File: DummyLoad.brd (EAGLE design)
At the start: 101.6 x 76.2 mm, 16 parts, among them IC1 LM358, J1 BINDING-POST, J2 BINDING-POST, Q1 NTE2390-OFFBOARD, SW1 SWITCH-SPDT, X1 SCREW-TERM-2

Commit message: Rough layout
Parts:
- removed X1: SCREW-TERM-2, SaintGimp:SCREW-TERM-2
- added C4: 100uF, SaintGimp:CAP-POL-5-8
- added C5: 2.2uF, SaintGimp:CAP-POL-2.5-5
- added D1: LED, SaintGimp:LED5MM
- added J10, J3, J4, J5, J7, J8, J9: PINHD-1X1, SaintGimp:1X01
- added J6: POWERJACK-OFFBRD, SaintGimp:1X03
- added R10: 47K, SaintGimp:AXIAL-7.5MM
- added R7: 1M, SaintGimp:AXIAL-7.5MM
- added R8: 4K7, SaintGimp:AXIAL-7.5MM
- added R9: (no value), SaintGimp:AXIAL-7.5MM
- added RV2, RV3: 5K, SaintGimp:TRIM_POT
- added SW2: SWITCH-SPDT-OFFBRD, SaintGimp:1X03
- added U$1: PANEL-METER-OFFBRD, SaintGimp:1X04
- added U1: LP2950, SaintGimp:TO92-INLINE
- Q1: value NTE2390-OFFBOARD -> NTE2390; device SaintGimp:SCREW-TERM-3 -> SaintGimp:TO220BV
- R3: value 12K -> 180K
- R4: value 3.3K -> 4K7
- R5: value 1R -> 0R1; device SaintGimp:SCREW-TERM-2 -> SaintGimp:AXIAL-7.5MM
- R6: value 150R -> 68K
- RV1: device SaintGimp:POT-PCB-MOUNT -> SaintGimp:1X03
- SW1: value SWITCH-SPDT -> SWITCH-SPDT-OFFBRD; device SaintGimp:SWITCH-SPDT -> SaintGimp:1X03
- moved R4 65.9 mm to (11.4, 10.2)
- moved R3 54.6 mm to (30.5, 11.4), turned to 90 degrees
- moved J1 50.2 mm to (59.7, 11.4)
- moved J2 50.2 mm to (58.4, 33.0)
- moved R2 41.6 mm to (33.0, 11.4), turned to 90 degrees
- moved R1 39.5 mm to (11.4, 12.7), turned to 180 degrees
- moved SW1 37.4 mm to (17.8, 3.81)
- moved R6 37.1 mm to (11.4, 20.3)
- moved C1 35.9 mm to (21.6, 7.62)
- moved Q1 31.0 mm to (76.2, 26.7), turned to 270 degrees
- moved IC1 27.3 mm to (22.9, 14.0)
- moved R5 26.9 mm to (74.9, 15.2)
- moved C3 19.0 mm to (35.6, 11.4), turned to 270 degrees
- moved C2 18.1 mm to (21.6, 20.3)
- moved RV1 8.03 mm to (38.1, 3.81), turned to 0 degrees
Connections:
- removed net N$2 (its old number): Q1.1, R1.P$2
- new net +5V: C2.1, C5.+, D1.A, IC1.8, J7.1, RV1.3, U$1.1, U1.1
- new net GATE: J3.1, Q1.P1, R1.P$2, R7.P$1
- new net METER: IC1.7, J10.1, R6.P$2, U$1.3
- new net N$12: R8.P$1, RV3.2
- new net N$13: IC1.3, R3.P$2, SW1.2
- new net N$4: D1.K, R9.P$1
- new net SENSE: IC1.5, J4.1, Q1.P3, R2.P$2, R5.P$2
- net GND: now also C4.-, C5.-, J5.1, J6.2, J6.3, J8.1, J9.1, R10.P$1, R5.P$1, R7.P$2, R9.P$2, RV1.1, RV2.1, RV2.3, RV3.1, RV3.3, U$1.2, U$1.4, U1.2; no longer IC1.5, R5.1, R6.P$1, RV1.P$1, X1.2
- net N$1: now also J6.1, SW2.2; no longer IC1.6, IC1.7
- net N$10: now also R4.P$2; no longer R3.P$1, RV1.P$2
- net N$11: now also RV2.2; no longer R6.P$2
- net N$3: now also C4.+, SW2.3, U1.3; no longer Q1.3, R2.P$2, R5.2
- net N$6: now also C3.1, R3.P$1, RV1.2; no longer R3.P$2, R4.P$2, SW1.1
- net N$7: now also Q1.P2; no longer Q1.2
- net N$8: now also IC1.6, R6.P$1, R8.P$2; no longer C2.1, IC1.8, RV1.P$3, X1.1
- net N$9: now also R10.P$2, SW1.1; no longer C3.1, IC1.3, SW1.2
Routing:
- net +5V: track 0.00 -> 66.5 mm
- net N$11: track 0.00 -> 59.0 mm
- net METER: track 0.00 -> 45.4 mm
- net N$13: track 0.00 -> 32.4 mm
- net SENSE: track 0.00 -> 21.8 mm
- net N$8: track 0.00 -> 19.7 mm
- net N$6: track 0.00 -> 17.5 mm
- net N$3: track 0.00 -> 13.9 mm
- net N$5: track 0.00 -> 13.7 mm
- net GATE: track 0.00 -> 13.2 mm
- net N$1: track 0.00 -> 12.4 mm
- net N$10: track 0.00 -> 8.45 mm
- net N$7: track 0.00 -> 8.44 mm
- net N$2: track 0.00 -> 7.52 mm
- net N$12: track 0.00 -> 7.42 mm
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- added copper zone on layer 16, net GND
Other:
- board size 101.6 x 76.2 mm -> 48.3 x 39.4 mm

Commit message: Second layout pass
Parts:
- removed U$1: PANEL-METER-OFFBRD, SaintGimp:1X04
- added PM1: PANEL-METER-OFFBRD, SaintGimp:1X04
- R9: value (none) -> 330
- moved J7 34.2 mm to (15.2, 31.8)
- moved J9 30.2 mm to (12.7, 31.8)
- moved J8 29.7 mm to (17.8, 31.8)
- moved J4 29.3 mm to (12.7, 3.81)
- moved J5 16.5 mm to (15.2, 3.81)
- moved J10 10.9 mm to (10.2, 31.8)
- moved RV1 5.08 mm to (33.0, 3.81)
- moved J6 4.58 mm to (24.1, 31.8)
- moved SW2 4.58 mm to (33.0, 31.8)
- moved SW1 3.81 mm to (21.6, 3.81)
- moved J3 1.27 mm to (10.2, 3.81)
- turned R1 to 0 degrees
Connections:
- net +5V: now also PM1.1; no longer U$1.1
- net GATE: now also R1.P$1; no longer R1.P$2
- net GND: now also PM1.2, PM1.4; no longer U$1.2, U$1.4
- net METER: now also PM1.3; no longer U$1.3
- net N$2: now also R1.P$2; no longer R1.P$1
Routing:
- net GND: track 5.25 -> 43.4 mm
- net N$11: track 59.0 -> 29.0 mm
- net SENSE: track 21.8 -> 38.0 mm
- net N$13: track 32.4 -> 20.6 mm
- net METER: track 45.4 -> 33.9 mm
- net +5V: track 66.5 -> 59.8 mm
- net N$10: track 8.45 -> 13.7 mm
- net N$3: track 13.9 -> 9.94 mm
- net N$9: track 3.81 -> 5.39 mm
- net N$6: track 17.5 -> 16.1 mm
- net GATE: track 13.2 -> 12.6 mm

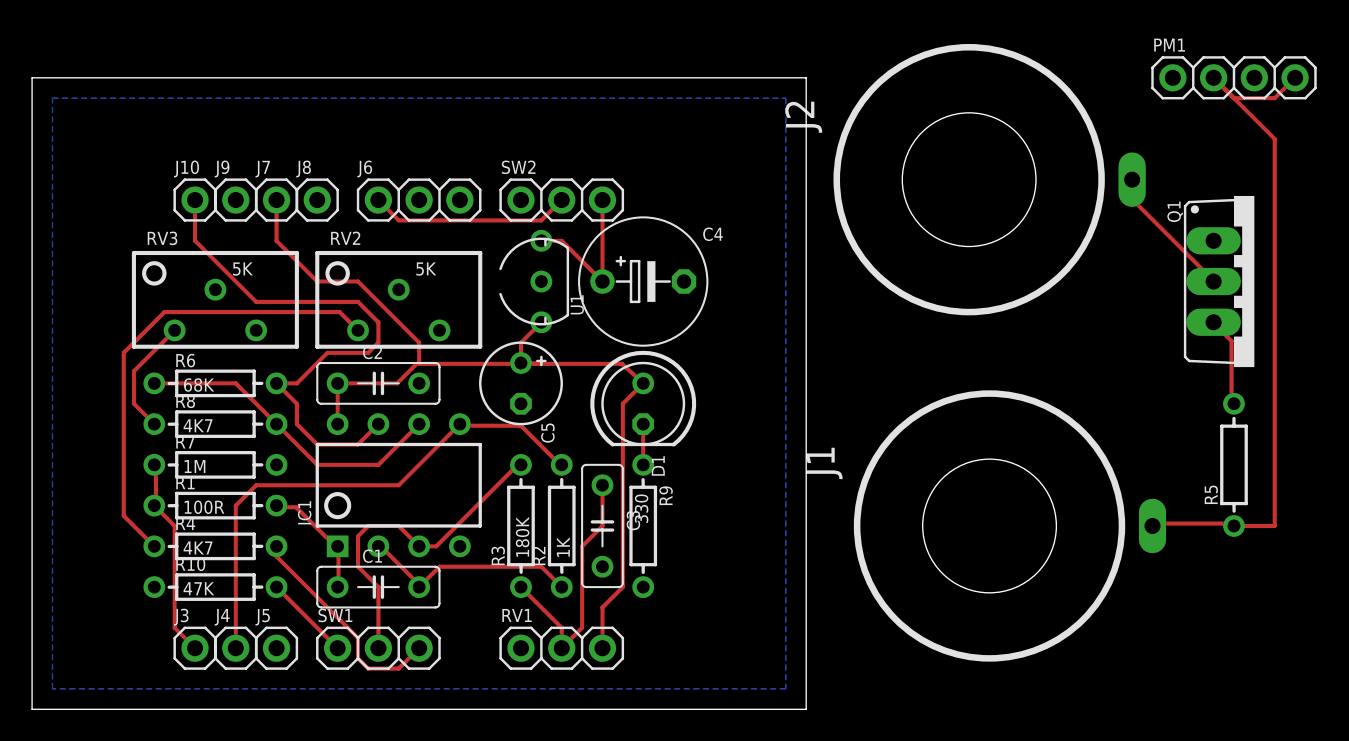
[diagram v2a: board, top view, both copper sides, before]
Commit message: Add silk screen
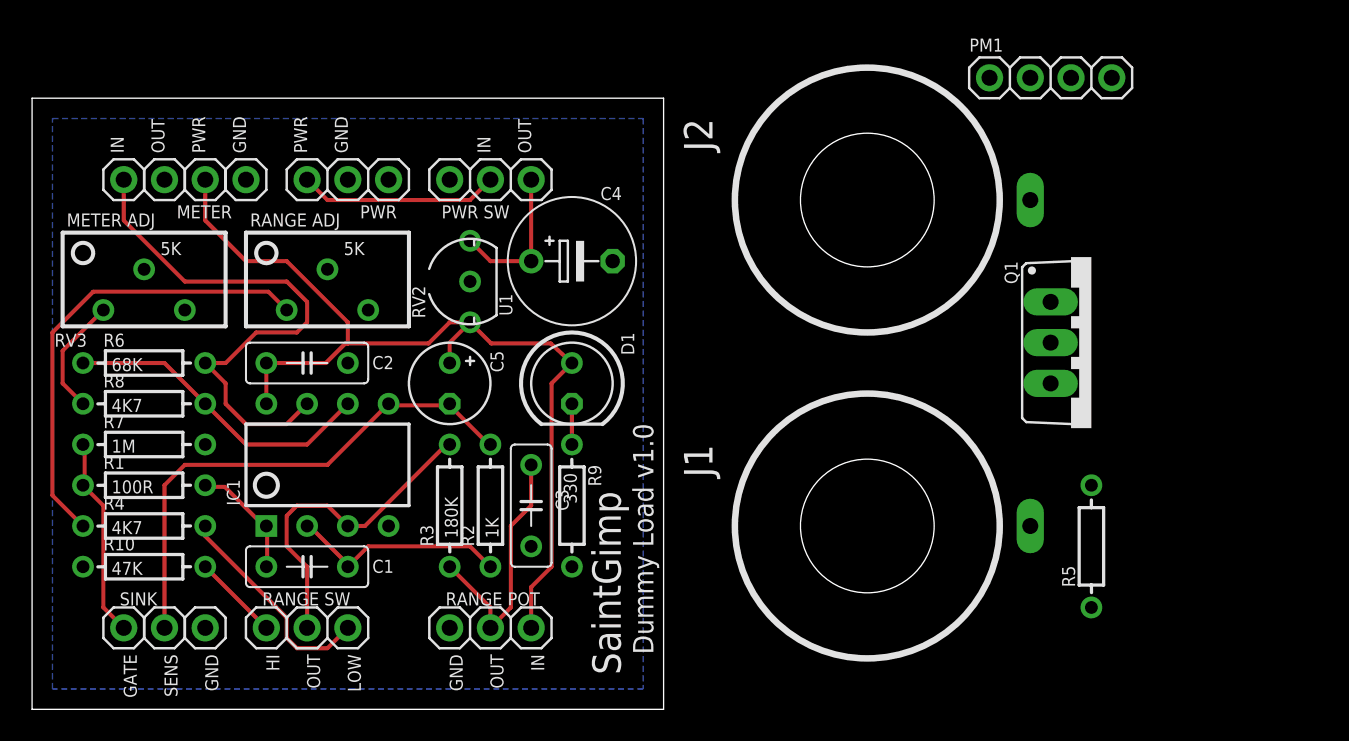
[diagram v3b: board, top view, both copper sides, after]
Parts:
- moved PM1 11.4 mm to (63.5, 39.4)
- moved Q1 10.9 mm to (66.0, 22.9)
- moved R5 10.2 mm to (66.0, 10.2)
- moved J1 7.62 mm to (52.1, 11.4)
- moved J2 6.48 mm to (52.1, 31.8)
- moved SW2 4.62 mm to (28.6, 33.0)
- moved C3 4.62 mm to (31.1, 12.7)
- moved R2 4.62 mm to (28.6, 12.7)
- moved RV1 4.62 mm to (28.6, 5.08)
- moved J10 4.62 mm to (5.71, 33.0)
- moved J6 4.62 mm to (19.7, 33.0)
- moved J7 4.62 mm to (10.8, 33.0)
- moved J8 4.62 mm to (13.3, 33.0)
- moved RV2 4.62 mm to (18.4, 26.7)
- moved C1 4.62 mm to (17.1, 8.89)
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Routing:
- net GND: track 43.4 -> 0.00 mm
- net N$7: track 8.44 -> 0.00 mm
- net SENSE: track 38.0 -> 32.4 mm
- net N$3: track 9.94 -> 9.42 mm
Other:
- board size 48.3 x 39.4 mm -> 39.4 x 38.1 mm
- board text added: "Dummy Load v1.0"
- board text added: "GATE"
- board text added: "GND"
- board text added: "HI"
- board text added: "IN"
- board text added: "LOW"
- board text added: "METER"
- board text added: "METER ADJ"
- board text added: "OUT"
- board text added: "PWR"
- board text added: "PWR SW"
- board text added: "RANGE ADJ"
- board text added: "RANGE POT"
- board text added: "RANGE SW"
- board text added: "SENS"
- board text added: "SINK"
- board text added: "SaintGimp"

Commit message: Tweak values
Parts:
- removed R7: 1M, SaintGimp:AXIAL-7.5MM
- C1: value 0.1uF -> 22nF
- C4: device SaintGimp:CAP-POL-5-8 -> SaintGimp:CAP-POL-2.5-5
- R1: value 100R -> 470R
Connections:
- net GATE: no longer R7.P$1
- net GND: no longer R7.P$2
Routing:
- net GATE: track 12.6 -> 10.1 mm
- net N$3: track 9.42 -> 10.8 mm
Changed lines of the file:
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@@
 <?xml version="1.0" encoding="utf-8"?>
 <!DOCTYPE eagle SYSTEM "eagle.dtd">
-<eagle version="7.2.0">
+<eagle version="7.4.0">
 <drawing>
 <settings>
@@
 <layer number="56" name="wert" color="7" fill="1" visible="no" active="no"/>
 <layer number="57" name="tCAD" color="7" fill="1" visible="no" active="no"/>
+<layer number="59" name="tCarbon" color="7" fill="1" visible="no" active="no"/>
+<layer number="60" name="bCarbon" color="7" fill="1" visible="no" active="no"/>
 <layer number="90" name="Modules" color="5" fill="1" visible="no" active="no"/>
 <layer number="91" name="Nets" color="2" fill="1" visible="no" active="no"/>
@@
 <layer number="113" name="IDFDebug" color="7" fill="1" visible="yes" active="yes"/>
 <layer number="116" name="Patch_BOT" color="9" fill="4" visible="yes" active="yes"/>
+<layer number="118" name="Rect_Pads" color="7" fill="1" visible="no" active="no"/>
 <layer number="121" name="_tsilk" color="7" fill="1" visible="yes" active="yes"/>
 <layer number="122" name="_bsilk" color="7" fill="1" visible="yes" active="yes"/>
@@
 <layer number="127" name="_tValues" color="7" fill="1" visible="yes" active="yes"/>
 <layer number="128" name="_bValues" color="7" fill="1" visible="yes" active="yes"/>
+<layer number="129" name="Mask" color="7" fill="1" visible="yes" active="yes"/>
 <layer number="131" name="tAdjust" color="7" fill="1" visible="yes" active="yes"/>
 <layer number="132" name="bAdjust" color="7" fill="1" visible="yes" active="yes"/>
@@
 <layer number="230" name="230bmp" color="7" fill="1" visible="yes" active="yes"/>
 <layer number="231" name="231bmp" color="7" fill="1" visible="yes" active="yes"/>
+<layer number="232" name="Eagle3D_PG2" color="7" fill="1" visible="no" active="no"/>
+<layer number="233" name="Eagle3D_PG3" color="7" fill="1" visible="no" active="no"/>
 <layer number="248" name="Housing" color="7" fill="1" visible="yes" active="yes"/>
 <layer number="249" name="Edge" color="7" fill="1" visible="yes" active="yes"/>
@@
 <attribute name="PROD_ID" value="IC-09172" x="18.415" y="15.24" size="1.778" layer="27" display="off"/>
 </element>
-<element name="R1" library="SaintGimp" package="AXIAL-7.5MM" value="100R" x="6.985" y="13.97"/>
+<element name="R1" library="SaintGimp" package="AXIAL-7.5MM" value="470R" x="6.985" y="13.97"/>
 <element name="R2" library="SaintGimp" package="AXIAL-7.5MM" value="1K" x="28.575" y="12.7" rot="R90"/>
 <element name="R3" library="SaintGimp" package="AXIAL-7.5MM" value="180K" x="26.035" y="12.7" rot="R90"/>
@@
 <attribute name="VALUE" value="" x="66.04" y="10.16" size="1.778" layer="27" rot="R90" display="off"/>
 </element>
-<element name="C1" library="SaintGimp" package="CAPACITOR-5MM" value="0.1uF" x="17.145" y="8.89" smashed="yes">
+<element name="C1" library="SaintGimp" package="CAPACITOR-5MM" value="22nF" x="17.145" y="8.89" smashed="yes">
 <attribute name="NAME" x="21.209" y="8.509" size="0.8128" layer="25"/>
 <attribute name="VALUE" x="15.24" y="6.604" size="0.8128" layer="27"/>
@@
 </element>
 <element name="U1" library="SaintGimp" package="TO92-INLINE" value="LP2950" x="27.305" y="26.67" rot="R90"/>
-<element name="C4" library="SaintGimp" package="CAP-POL-5-8" value="100uF" x="33.655" y="27.94" smashed="yes">
+<element name="C4" library="SaintGimp" package="CAP-POL-2.5-5" value="100uF" x="33.655" y="27.94" smashed="yes">
 <attribute name="NAME" x="35.433" y="31.75" size="0.8128" layer="25" ratio="10"/>
 <attribute name="VALUE" x="37.338" y="24.765" size="0.8128" layer="27" ratio="10"/>
@@
 <attribute name="VALUE" x="4.445" y="30.6491625" size="0.8128" layer="27"/>
 </element>
-<element name="R7" library="SaintGimp" package="AXIAL-7.5MM" value="1M" x="6.985" y="16.51"/>
 <element name="SW2" library="SaintGimp" package="1X03" value="SWITCH-SPDT-OFFBRD" x="28.575" y="33.02" smashed="yes">
 <attribute name="VALUE" x="24.765" y="30.6491625" size="0.8128" layer="27"/>
@@
 <contactref element="J8" pad="1"/>
 <contactref element="J9" pad="1"/>
-<contactref element="R7" pad="P$2"/>
 <contactref element="RV3" pad="3"/>
 <contactref element="RV3" pad="1"/>
@@
 <wire x1="62.23" y1="11.43" x2="62.23" y2="39.37" width="0" layer="19" extent="1-1"/>
 <wire x1="66.04" y1="6.35" x2="62.23" y2="11.43" width="0" layer="19" extent="1-1"/>
-<wire x1="36.195" y1="27.94" x2="62.23" y2="39.37" width="0" layer="19" extent="1-1"/>
+<wire x1="34.925" y1="27.94" x2="62.23" y2="39.37" width="0" layer="19" extent="1-1"/>
+<wire x1="27.305" y1="26.67" x2="34.925" y2="27.94" width="0" layer="19" extent="1-1"/>
+<wire x1="20.955" y1="24.892" x2="27.305" y2="26.67" width="0" layer="19" extent="1-1"/>
+<wire x1="19.685" y1="21.59" x2="20.955" y2="24.892" width="0" layer="19" extent="1-1"/>
+<wire x1="18.415" y1="27.432" x2="20.955" y2="24.892" width="0" layer="19" extent="1-1"/>
+<wire x1="19.685" y1="33.02" x2="18.415" y2="27.432" width="0" layer="19" extent="1-1"/>
+<wire x1="22.225" y1="33.02" x2="19.685" y2="33.02" width="0" layer="19" extent="1-1"/>
+<wire x1="13.335" y1="33.02" x2="19.685" y2="33.02" width="0" layer="19" extent="1-1"/>
+<wire x1="8.255" y1="33.02" x2="13.335" y2="33.02" width="0" layer="19" extent="1-1"/>
+<wire x1="6.985" y1="27.432" x2="8.255" y2="33.02" width="0" layer="19" extent="1-1"/>
+<wire x1="9.525" y1="24.892" x2="6.985" y2="27.432" width="0" layer="19" extent="1-1"/>
+<wire x1="26.035" y1="19.05" x2="19.685" y2="21.59" width="0" layer="19" extent="1-1"/>
+<wire x1="22.225" y1="11.43" x2="26.035" y2="19.05" width="0" layer="19" extent="1-1"/>
+<wire x1="26.035" y1="5.08" x2="22.225" y2="11.43" width="0" layer="19" extent="1-1"/>
+<wire x1="31.115" y1="10.16" x2="26.035" y2="5.08" width="0" layer="19" extent="1-1"/>
+<wire x1="33.655" y1="8.89" x2="31.115" y2="10.16" width="0" layer="19" extent="1-1"/>
+<wire x1="10.795" y1="5.08" x2="22.225" y2="11.43" width="0" layer="19" extent="1-1"/>
+<wire x1="3.175" y1="8.89" x2="10.795" y2="5.08" width="0" layer="19" extent="1-1"/>
 </signal>
 <signal name="GATE">
@@
 <contactref element="R1" pad="P$1"/>
 <contactref element="J3" pad="1"/>
-<contactref element="R7" pad="P$1"/>
-<wire x1="3.2766" y1="16.51" x2="3.2766" y2="14.0716" width="0.254" layer="1"/>
+<wire x1="3.2766" y1="16.51" x2="3.2766" y2="14.0716" width="0" layer="19" extent="1-16"/>
 <wire x1="3.2766" y1="14.0716" x2="3.175" y2="13.97" width="0.254" layer="1"/>
-<wire x1="3.2766" y1="16.51" x2="3.175" y2="16.51" width="0.254" layer="1"/>
 <wire x1="4.445" y1="6.35" x2="4.445" y2="12.7" width="0.254" layer="1"/>
 <wire x1="4.445" y1="12.7" x2="3.175" y2="13.97" width="0.254" layer="1"/>
@@
 <contactref element="C4" pad="+"/>
 <contactref element="SW2" pad="3"/>
-<wire x1="31.115" y1="33.02" x2="31.115" y2="27.94" width="0.254" layer="1"/>
+<wire x1="31.115" y1="33.02" x2="32.385" y2="27.94" width="0.254" layer="1"/>
 <wire x1="27.305" y1="29.21" x2="28.575" y2="27.94" width="0.254" layer="1"/>
-<wire x1="28.575" y1="27.94" x2="31.115" y2="27.94" width="0.254" layer="1"/>
+<wire x1="28.575" y1="27.94" x2="32.385" y2="27.94" width="0.254" layer="1"/>
 </signal>
 <signal name="METER">

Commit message: Clean up layout
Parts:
- C4: device SaintGimp:CAP-POL-2.5-5 -> SaintGimp:CAP-POL-2.5-6
- moved J3 2.54 mm to (8.26, 5.08)
- moved J5 2.54 mm to (13.3, 5.08)
- moved J4 2.54 mm to (10.8, 5.08)
- moved SW1 2.54 mm to (19.7, 5.08)
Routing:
- net N$10: track 13.7 -> 17.5 mm
- net N$9: track 5.39 -> 7.93 mm
- net +5V: track 59.7 -> 57.3 mm
- net GATE: track 10.1 -> 11.5 mm
- net SENSE: track 32.4 -> 33.6 mm
- net N$13: track 20.6 -> 21.7 mm
